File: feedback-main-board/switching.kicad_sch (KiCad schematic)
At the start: 35 parts

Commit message: wip
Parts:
- removed Q?: MMBT3906, Package_TO_SOT_SMD:SOT-23, symbol Transistor_BJT:MMBT3906
- added C?: 100n, symbol Device:C
- added Q?: MMBT3904, Package_TO_SOT_SMD:SOT-23, symbol Transistor_BJT:MMBT3904
- added R? (x2): 10k, Resistor_SMD:R_0603_1608Metric_Pad0.98x0.95mm_HandSolder, symbol Device:R
- added U?: DG403, Package_SO:SOIC-16_3.9x9.9mm_P1.27mm, symbol pedals:DG403 Fixed
- R?: value 100k -> 10k
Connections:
- net +4V5: now also U?.13 (GND)
- net +9V: now also R?.1, C?.1, U?.11 (V+), U?.12 (VL)
- net BypassState: now also R?.1, R?.1; no longer U?.6 (D4), U?.8 (D2)
- net GND: now also C?.2, Q?.2 (E), U?.14 (V-); no longer R?.2
- net LatchStateInv: now also R?.2, Q?.3 (C); no longer R?.1
- net at R?.2: now also Q?.1 (B)
- new net: R?.2, U?.8 (D2)
- new net: R?.2, U?.6 (D4)
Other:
- moved on the sheet: R?

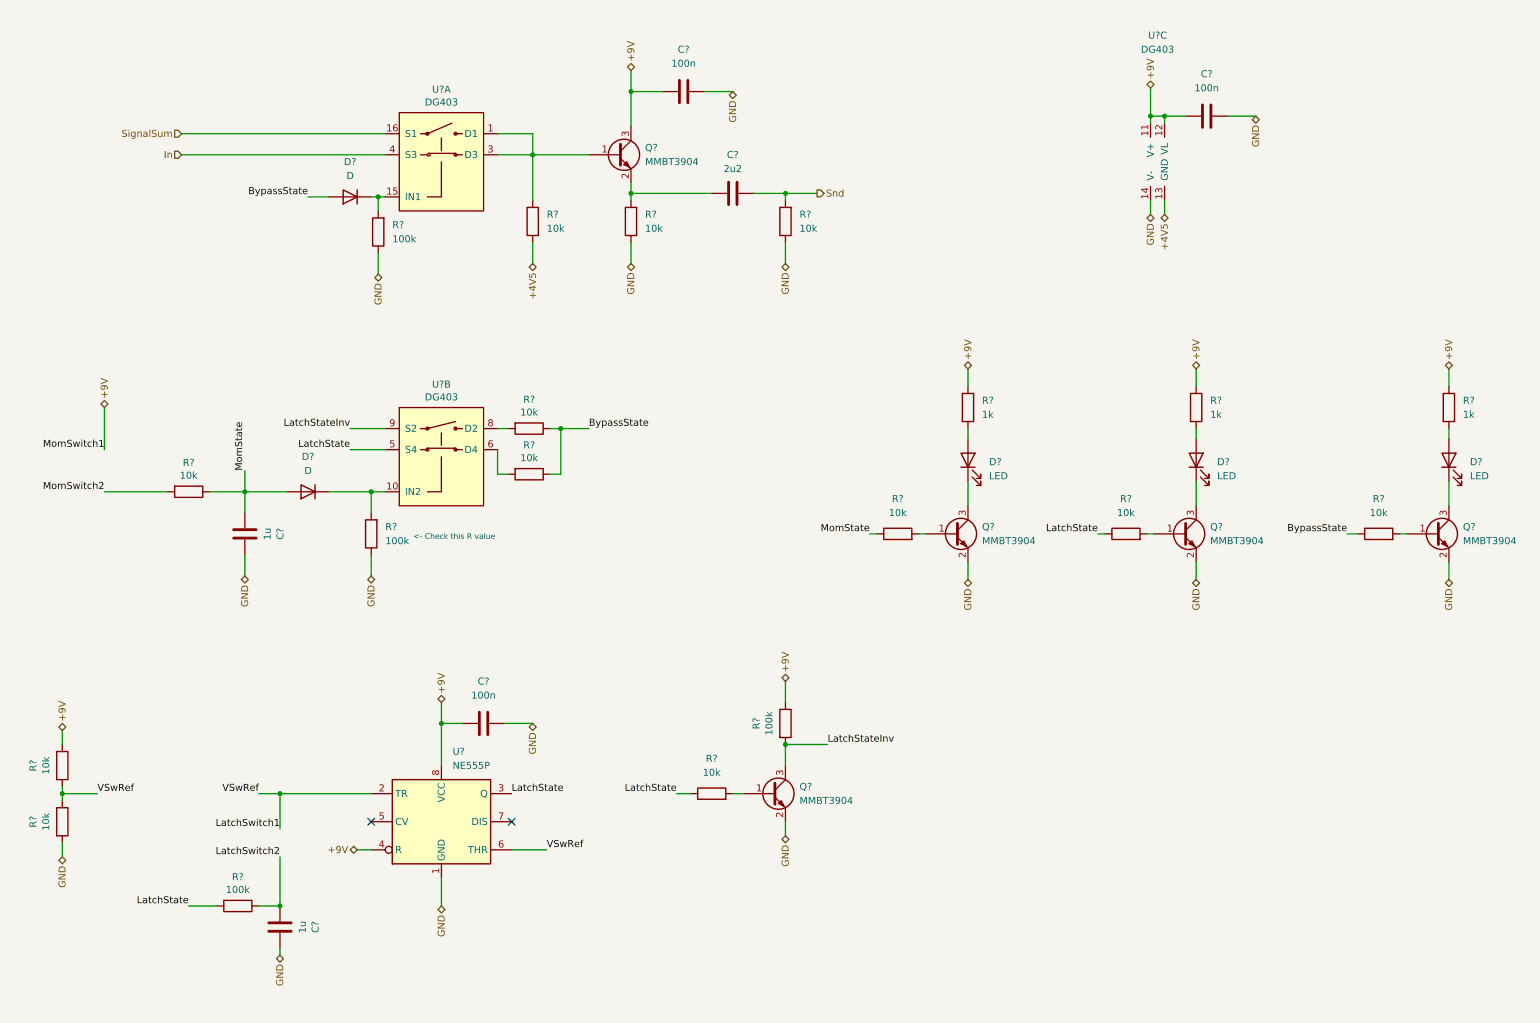
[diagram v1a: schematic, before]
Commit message: Switching fixes from breadboarding pre-CD4070
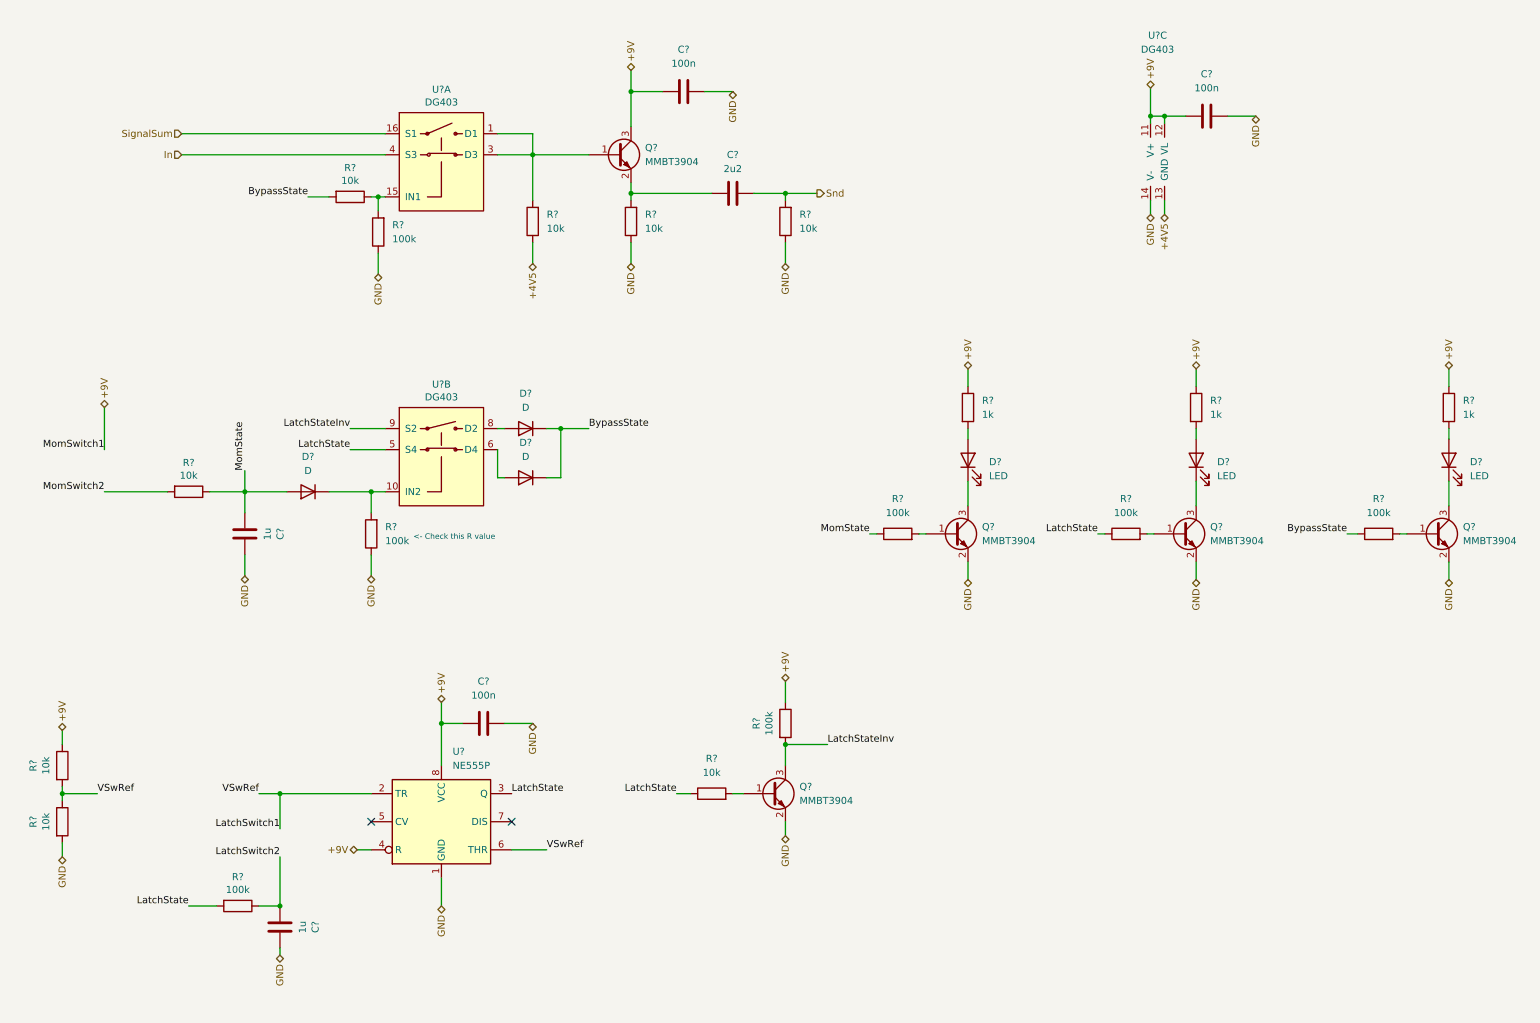
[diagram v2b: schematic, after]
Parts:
- removed D?: D, symbol Device:D
- removed R?: 10k, Resistor_SMD:R_0603_1608Metric_Pad0.98x0.95mm_HandSolder, symbol Device:R
- added D? (x2): D, symbol Device:D
- R? (x3): value 10k -> 100k
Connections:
- net BypassState: now also R?.2, D?.1 (K), D?.1 (K); no longer R?.1
- net at R?.2, U?.15 (IN1): now also R?.1
- net at U?.8 (D2): now also D?.2 (A); no longer R?.2
- net at U?.6 (D4): now also D?.2 (A)
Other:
- moved on the sheet: R?
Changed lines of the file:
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@@
   (junction (at 151.13 50.165) (diameter 0) (color 0 0 0 0)
   )
+  (junction (at 59.69 179.07) (diameter 0) (color 0 0 0 0)
+  )
+  (junction (at 123.19 31.75) (diameter 0) (color 0 0 0 0)
+  )
   (junction (at 110.49 92.71) (diameter 0) (color 0 0 0 0)
-  )
-  (junction (at 59.69 179.07) (diameter 0) (color 0 0 0 0)
-  )
-  (junction (at 123.19 31.75) (diameter 0) (color 0 0 0 0)
   )
   (junction (at 53.34 104.14) (diameter 0) (color 0 0 0 0)
@@
     (stroke (width 0) (type default) (color 0 0 0 0))
   )
+  (wire (pts (xy 99.06 92.71) (xy 100.33 92.71))
+    (stroke (width 0) (type default) (color 0 0 0 0))
+  )
   (wire (pts (xy 184.15 81.915) (xy 184.15 85.09))
     (stroke (width 0) (type default) (color 0 0 0 0))
@@
     (stroke (width 0) (type default) (color 0 0 0 0))
   )
+  (wire (pts (xy 100.33 101.6) (xy 99.06 101.6))
+    (stroke (width 0) (type default) (color 0 0 0 0))
+  )
   (wire (pts (xy 225.425 81.915) (xy 225.425 85.09))
     (stroke (width 0) (type default) (color 0 0 0 0))
@@
     (stroke (width 0) (type default) (color 0 0 0 0))
   )
-  (wire (pts (xy 110.49 92.71) (xy 110.49 100.965))
+  (wire (pts (xy 110.49 92.71) (xy 110.49 101.6))
     (stroke (width 0) (type default) (color 0 0 0 0))
   )
@@
     (stroke (width 0) (type default) (color 0 0 0 0))
   )
-  (wire (pts (xy 99.06 92.71) (xy 100.965 92.71))
-    (stroke (width 0) (type default) (color 0 0 0 0))
-  )
   (wire (pts (xy 225.425 92.71) (xy 225.425 94.615))
     (stroke (width 0) (type default) (color 0 0 0 0))
   )
+  (wire (pts (xy 107.95 92.71) (xy 110.49 92.71))
+    (stroke (width 0) (type default) (color 0 0 0 0))
+  )
   (wire (pts (xy 41.91 39.37) (xy 78.74 39.37))
     (stroke (width 0) (type default) (color 0 0 0 0))
@@
     (stroke (width 0) (type default) (color 0 0 0 0))
   )
-  (wire (pts (xy 108.585 92.71) (xy 110.49 92.71))
-    (stroke (width 0) (type default) (color 0 0 0 0))
-  )
   (wire (pts (xy 100.33 146.05) (xy 105.41 146.05))
     (stroke (width 0) (type default) (color 0 0 0 0))
@@
     (stroke (width 0) (type default) (color 0 0 0 0))
   )
-  (wire (pts (xy 99.06 96.52) (xy 99.06 100.965))
+  (wire (pts (xy 99.06 96.52) (xy 99.06 101.6))
     (stroke (width 0) (type default) (color 0 0 0 0))
   )
@@
     (stroke (width 0) (type default) (color 0 0 0 0))
   )
-  (wire (pts (xy 108.585 100.965) (xy 110.49 100.965))
-    (stroke (width 0) (type default) (color 0 0 0 0))
-  )
   (wire (pts (xy 77.47 60.96) (xy 77.47 64.77))
     (stroke (width 0) (type default) (color 0 0 0 0))
@@
     (stroke (width 0) (type default) (color 0 0 0 0))
   )
-  (wire (pts (xy 99.06 100.965) (xy 100.965 100.965))
-    (stroke (width 0) (type default) (color 0 0 0 0))
-  )
   (wire (pts (xy 123.19 31.75) (xy 128.905 31.75))
     (stroke (width 0) (type default) (color 0 0 0 0))
@@
   )
   (wire (pts (xy 151.13 149.86) (xy 158.75 149.86))
+    (stroke (width 0) (type default) (color 0 0 0 0))
+  )
+  (wire (pts (xy 107.95 101.6) (xy 110.49 101.6))
     (stroke (width 0) (type default) (color 0 0 0 0))
   )
@@
     )
     (property "Mouser" "80-C0603C105K9PLR" (id 4) (at 59.69 182.88 0)
+      (effects (font (size 1.27 1.27)) hide)
+    )
+    (pin "1")
+    (pin "2")
+  )
+  (symbol (lib_id "Device:D") (at 104.14 101.6 180) (unit 1)
+    (in_bom yes) (on_board yes) (fields_autoplaced)
+    (property "Reference" "D?" (id 0) (at 104.14 95.25 0))
+    (property "Value" "D" (id 1) (at 104.14 97.79 0))
+    (property "Footprint" "" (id 2) (at 104.14 101.6 0)
+      (effects (font (size 1.27 1.27)) hide)
+    )
+    (property "Datasheet" "~" (id 3) (at 104.14 101.6 0)
       (effects (font (size 1.27 1.27)) hide)
     )
@@
     (in_bom yes) (on_board yes) (fields_autoplaced)
     (property "Reference" "R?" (id 0) (at 212.725 105.41 90))
-    (property "Value" "10k" (id 1) (at 212.725 107.95 90))
+    (property "Value" "100k" (id 1) (at 212.725 107.95 90))
     (property "Footprint" "" (id 2) (at 212.725 113.538 90)
       (effects (font (size 1.27 1.27)) hide)
@@
     (pin "2")
   )
+  (symbol (lib_id "Device:D") (at 104.14 92.71 180) (unit 1)
+    (in_bom yes) (on_board yes) (fields_autoplaced)
+    (property "Reference" "D?" (id 0) (at 104.14 86.36 0))
+    (property "Value" "D" (id 1) (at 104.14 88.9 0))
+    (property "Footprint" "" (id 2) (at 104.14 92.71 0)
+      (effects (font (size 1.27 1.27)) hide)
+    )
+    (property "Datasheet" "~" (id 3) (at 104.14 92.71 0)
+      (effects (font (size 1.27 1.27)) hide)
+    )
+    (pin "1")
+    (pin "2")
+  )
   (symbol (lib_id "Device:C") (at 96.52 146.05 90) (unit 1)
     (in_bom yes) (on_board yes) (fields_autoplaced)
@@
     (in_bom yes) (on_board yes) (fields_autoplaced)
     (property "Reference" "R?" (id 0) (at 171.45 105.41 90))
-    (property "Value" "10k" (id 1) (at 171.45 107.95 90))
+    (property "Value" "100k" (id 1) (at 171.45 107.95 90))
     (property "Footprint" "" (id 2) (at 171.45 113.538 90)
       (effects (font (size 1.27 1.27)) hide)
@@
     (pin "14")
   )
-  (symbol (lib_id "Device:R") (at 104.775 92.71 270) (unit 1)
+  (symbol (lib_id "Device:R") (at 72.39 50.8 270) (unit 1)
     (in_bom yes) (on_board yes)
-    (property "Reference" "R?" (id 0) (at 104.775 87.4522 90))
-    (property "Value" "10k" (id 1) (at 104.775 89.7636 90))
-    (property "Footprint" "Resistor_SMD:R_0603_1608Metric_Pad0.98x0.95mm_HandSolder" (id 2) (at 104.775 90.932 90)
-      (effects (font (size 1.27 1.27)) hide)
-    )
-    (property "Datasheet" "~" (id 3) (at 104.775 92.71 0)
-      (effects (font (size 1.27 1.27)) hide)
-    )
-    (property "Mouser" "603-RT0603DRE07100KL" (id 4) (at 104.775 92.71 0)
+    (property "Reference" "R?" (id 0) (at 72.39 45.5422 90))
+    (property "Value" "10k" (id 1) (at 72.39 47.8536 90))
+    (property "Footprint" "Resistor_SMD:R_0603_1608Metric_Pad0.98x0.95mm_HandSolder" (id 2) (at 72.39 49.022 90)
+      (effects (font (size 1.27 1.27)) hide)
+    )
+    (property "Datasheet" "~" (id 3) (at 72.39 50.8 0)
+      (effects (font (size 1.27 1.27)) hide)
+    )
+    (property "Mouser" "603-RT0603DRE07100KL" (id 4) (at 72.39 50.8 0)
       (effects (font (size 1.27 1.27)) hide)
     )
@@
     (in_bom yes) (on_board yes) (fields_autoplaced)
     (property "Reference" "R?" (id 0) (at 258.445 105.41 90))
-    (property "Value" "10k" (id 1) (at 258.445 107.95 90))
+    (property "Value" "100k" (id 1) (at 258.445 107.95 90))
     (property "Footprint" "" (id 2) (at 258.445 113.538 90)
       (effects (font (size 1.27 1.27)) hide)
@@
     (pin "2")
   )
-  (symbol (lib_id "Device:R") (at 104.775 100.965 270) (unit 1)
-    (in_bom yes) (on_board yes)
-    (property "Reference" "R?" (id 0) (at 104.775 95.7072 90))
-    (property "Value" "10k" (id 1) (at 104.775 98.0186 90))
-    (property "Footprint" "Resistor_SMD:R_0603_1608Metric_Pad0.98x0.95mm_HandSolder" (id 2) (at 104.775 99.187 90)
-      (effects (font (size 1.27 1.27)) hide)
-    )
-    (property "Datasheet" "~" (id 3) (at 104.775 100.965 0)
-      (effects (font (size 1.27 1.27)) hide)
-    )
-    (property "Mouser" "603-RT0603DRE07100KL" (id 4) (at 104.775 100.965 0)
-      (effects (font (size 1.27 1.27)) hide)
-    )
-    (pin "1")
-    (pin "2")
-  )
   (symbol (lib_id "Device:R") (at 123.19 55.245 180) (unit 1)
     (in_bom yes) (on_board yes) (fields_autoplaced)
@@
       (effects (font (size 1.27 1.27)) hide)
     )
-    (pin "1")
-    (pin "2")
-  )
-  (symbol (lib_id "Device:D") (at 72.39 50.8 180) (unit 1)
-    (in_bom yes) (on_board yes) (fields_autoplaced)
-    (property "Reference" "D?" (id 0) (at 72.39 44.45 0))
-    (property "Value" "D" (id 1) (at 72.39 46.99 0))
-    (property "Footprint" "" (id 2) (at 72.39 50.8 0)
-      (effects (font (size 1.27 1.27)) hide)
-    )
-    (property "Datasheet" "~" (id 3) (at 72.39 50.8 0)
-      (effects (font (size 1.27 1.27)) hide)
-    )

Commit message: Board started
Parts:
- removed C?: 100n, symbol Device:C
- removed C?: 1u, Capacitor_SMD:C_0603_1608Metric_Pad1.08x0.95mm_HandSolder, symbol Device:C
- removed D? (x3): D, symbol Device:D
- removed Q? (x2): MMBT3904, Package_TO_SOT_SMD:SOT-23, symbol Transistor_BJT:MMBT3904
- removed R? (x2): 100k, symbol Device:R
- removed R? (x2): 10k, symbol Device:R
- removed R?: 100k, Resistor_SMD:R_0603_1608Metric_Pad0.98x0.95mm_HandSolder, symbol Device:R
- removed R?: 10k, Resistor_SMD:R_0603_1608Metric_Pad0.98x0.95mm_HandSolder, symbol Device:R
- added C19: 2u2, Capacitor_THT:C_Rect_L7.2mm_W7.2mm_P5.00mm_FKS2_FKP2_MKS2_MKP2, symbol Device:C
- added C20: 1u, Capacitor_SMD:C_0603_1608Metric_Pad1.08x0.95mm_HandSolder, symbol Device:C
- added C22: 100n, Capacitor_SMD:C_0603_1608Metric_Pad1.08x0.95mm_HandSolder, symbol Device:C
- added R23, R29, R30, R32: 10k, Resistor_SMD:R_0603_1608Metric_Pad0.98x0.95mm_HandSolder, symbol Device:R
- added R26, R27: 100, Resistor_SMD:R_0603_1608Metric_Pad0.98x0.95mm_HandSolder, symbol Device:R
- added R39: 100k, Resistor_SMD:R_0603_1608Metric_Pad0.98x0.95mm_HandSolder, symbol Device:R
- added U1: TL074, Package_SO:SOIC-14_3.9x8.7mm_P1.27mm, symbol Amplifier_Operational:TL074
- added U5: 4070, Package_SO:SOIC-14_3.9x8.7mm_P1.27mm, symbol 4xxx:4070
- C17, C21: renamed from C?; footprint (none) -> Capacitor_SMD:C_0603_1608Metric_Pad1.08x0.95mm_HandSolder
- C18: renamed from C?; footprint (none) -> Capacitor_THT:C_Rect_L7.2mm_W7.2mm_P5.00mm_FKS2_FKP2_MKS2_MKP2
- D6, D7, D8: renamed from D?; footprint (none) -> LED_THT:LED_D5.0mm
- R21, R31: renamed from R?; Mouser 603-RT0603DRE07100KL -> (none)
- R22, R28, R33, R35, R36: renamed from R?; footprint (none) -> Resistor_SMD:R_0603_1608Metric_Pad0.98x0.95mm_HandSolder; Mouser 603-RT0603DRE07100KL -> (none)
- R24, R25: renamed from R?; value 10k -> 100k; Mouser 603-RT0603DRE07100KL -> (none)
- R34, R37, R38: renamed from R?; footprint (none) -> Resistor_SMD:R_0603_1608Metric_Pad0.98x0.95mm_HandSolder
- gave numbers to parts that had none: 6
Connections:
- net +4V5: now also R23.1
- net +9V: now also C22.2, U5.14 (VDD)
- net BypassState: now also U3.10 (IN2), U3.15 (IN1), R32.1
- net GND: now also C20.2, C22.1, R29.1, R39.2, U5.12, U5.13, U5.5, U5.6, U5.7 (VSS), U5.8, U5.9
- net LatchState: now also R30.2; no longer U3.5 (S4)
- net MomState: now also C20.1, R39.1, U5.1
- net at U3.6 (D4): now also U3.8 (D2), R23.2, U1.12 (+)
- net at R22.2, U3.1 (D1), U3.3 (D3): now also U1.5 (+)
- net at C18.1: now also R26.2
- net LatchStateInv renamed FxOut
- net LatchSwitch1 renamed LatchSw1
- net LatchSwitch2 renamed LatchSw2
- net MomSwitch2 renamed MomSwIn
- new net: C19.1, R27.2
- new net: R26.1, U1.6 (-), U1.7
- new net: R27.1, U1.13 (-), U1.14
- new net: R32.2, U5.3
- new net: R30.1, U5.2
- new net Out: C19.2, R29.2
- new net RetBuf: U3.5 (S4)
- no-connect marks 2 -> 5
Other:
- note removed: "<- Check this R value"
- moved on the sheet: C16, C17, C18, C21, D6, D7, D8, Q2, Q3, Q4, R21, R22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

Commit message: Component placement
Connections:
- net at R23.2, U3.6 (D4), U3.8 (D2): now also U1.3 (+); no longer U1.12 (+)
- new net: R27.1, U1.1, U1.2 (-)
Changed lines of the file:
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@@
     (pin "2")
   )
-  (symbol (lib_id "Amplifier_Operational:TL074") (at 103.505 93.98 0) (mirror x) (unit 4)
+  (symbol (lib_id "Amplifier_Operational:TL074") (at 103.505 93.98 0) (mirror x) (unit 1)
     (in_bom yes) (on_board yes) (fields_autoplaced)
     (property "Reference" "U1" (id 0) (at 103.505 83.82 0))

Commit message: Mouser parts ordered
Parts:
- C16, C20: Mouser 80-C0603C105K9PLR -> 581-06035C105MAT2A
- C18, C19: Mouser (none) -> 505-MKS22.2/63/5
- U1: Mouser (none) -> 595-TL074IDR
- U4: Mouser 595-NE555DR -> 595-NE555PS
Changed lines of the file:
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@@
+      (effects (font (size 1.27 1.27)) hide)
+    )
+    (property "Mouser" "505-MKS22.2/63/5" (id 4) (at 133.35 93.98 0)
       (effects (font (size 1.27 1.27)) hide)
     )
@@
       (effects (font (size 1.27 1.27)) hide)
     )
-    (property "Mouser" "80-C0603C105K9PLR" (id 4) (at 40.005 185.42 0)
+    (property "Mouser" "581-06035C105MAT2A" (id 4) (at 40.005 185.42 0)
       (effects (font (size 1.27 1.27)) hide)
     )
@@
       (effects (font (size 1.27 1.27)) hide)
     )
-    (property "Mouser" "595-NE555DR" (id 4) (at 69.215 163.83 0)
+    (property "Mouser" "595-NE555PS" (id 4) (at 69.215 163.83 0)
       (effects (font (size 1.27 1.27)) hide)
     )
@@
       (effects (font (size 1.27 1.27)) hide)
     )
+    (property "Mouser" "505-MKS22.2/63/5" (id 4) (at 133.35 40.64 0)
+      (effects (font (size 1.27 1.27)) hide)
+    )
     (pin "1")
     (pin "2")
@@
       (effects (font (size 1.27 1.27)) hide)
     )
-    (property "Mouser" "80-C0603C105K9PLR" (id 4) (at 159.385 185.42 0)
+    (property "Mouser" "581-06035C105MAT2A" (id 4) (at 159.385 185.42 0)
       (effects (font (size 1.27 1.27)) hide)
     )
@@
       (effects (font (size 1.27 1.27)) hide)
     )
+    (property "Mouser" "595-TL074IDR" (id 4) (at 103.505 93.98 0)
+      (effects (font (size 1.27 1.27)) hide)
+    )
     (pin "1")
     (pin "2")
@@
       (effects (font (size 1.27 1.27)) hide)
     )
+    (property "Mouser" "595-TL074IDR" (id 4) (at 103.505 40.64 0)
+      (effects (font (size 1.27 1.27)) hide)
+    )

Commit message: Wip rev2
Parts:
- removed R31: 10k, Resistor_SMD:R_0603_1608Metric_Pad0.98x0.95mm_HandSolder, symbol Device:R
- added C23, C24: 100n, Capacitor_THT:C_Rect_L7.0mm_W2.5mm_P5.00mm, symbol Device:C
- added R40, R41: 100k, Resistor_SMD:R_0603_1608Metric_Pad0.98x0.95mm_HandSolder, symbol Device:R
- R24, R25: value 100k -> 10k
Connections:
- net MomState is gone; now on net MomSwIn: C20.1, R35.1, R39.1, U5.1
- net +4V5: now also R40.1, R41.1
- net at R22.2, U3.1 (D1), U3.3 (D3): now also C23.1; no longer U1.5 (+)
- net at R23.2, U3.6 (D4), U3.8 (D2): now also C24.1; no longer U1.3 (+)
- new net: C23.2, R40.2, U1.5 (+)
- new net: C24.2, R41.2, U1.3 (+)

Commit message: Changes pre-rev3
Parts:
- C16: LCSC (none) -> C15849
- C17, C21, C22: LCSC (none) -> C14663; Mouser (none) -> 581-06035C105MAT2A
- C18, C19, C23, C24, D6, D7, D8: LCSC (none) -> DNP
- C20: value 1u -> 100n; LCSC (none) -> C14663
- Q2, Q3, Q4: LCSC (none) -> C20526
- R21, R33, R35, R36, R39, R40, R41: LCSC (none) -> C25803
- R22, R23, R24, R25, R28, R29, R30, R32: LCSC (none) -> C25804
- R26, R27: LCSC (none) -> C22775
- R34, R37, R38: LCSC (none) -> C21190
- U1: LCSC (none) -> C6964
- U4: value NE555P -> NE555; LCSC (none) -> C7593; Mouser 595-NE555PS -> (none)
- U5: value 4070 -> CD4070; LCSC (none) -> C28329
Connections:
- net +4V5: no longer U3.13 (GND)
- net GND: now also U3.13 (GND)
